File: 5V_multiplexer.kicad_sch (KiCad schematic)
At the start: 7 parts, among them U13 PTPS2117DRLR

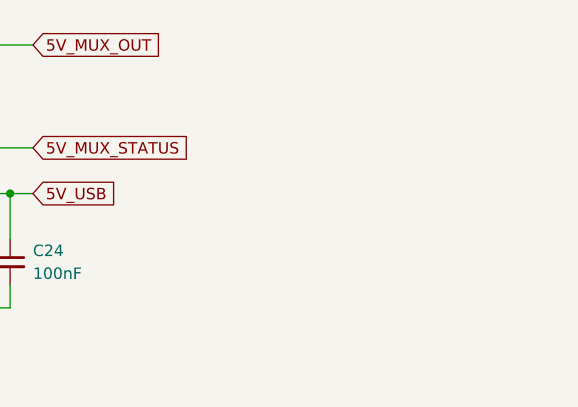
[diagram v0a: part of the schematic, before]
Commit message: updated components and nets
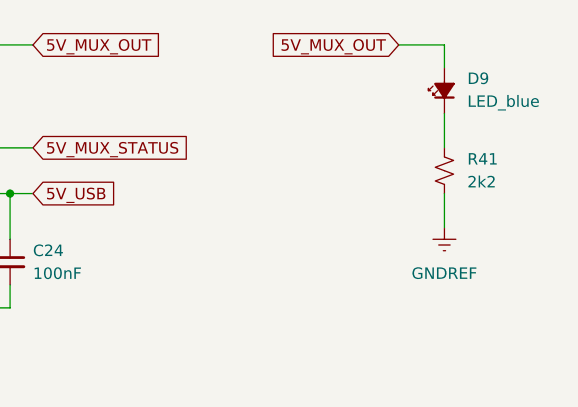
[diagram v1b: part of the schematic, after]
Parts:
- added D9: LED_blue, symbol Device:LED_Small_Filled
- added R41: 2k2, symbol Device:R_Small_US
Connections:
- net 5V_MUX_OUT: now also D9.2 (A)
- net GNDREF: now also R41.2
- new net: D9.1 (K), R41.1
